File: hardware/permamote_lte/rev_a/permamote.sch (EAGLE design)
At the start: 115 parts, among them IC1 NRF9160, J1 TC2030-JLINK-NL, J2 U.FL-R-SMT, J3 NANO_SIM, J4 U.FL-R-SMT, J5 DM3AT-SF-PEJM5, Q1 PMDXB950UPEL, Q10 PMDXB950UPEL, Q2 PMDXB950UPEL, Q3 PMDXB950UPEL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

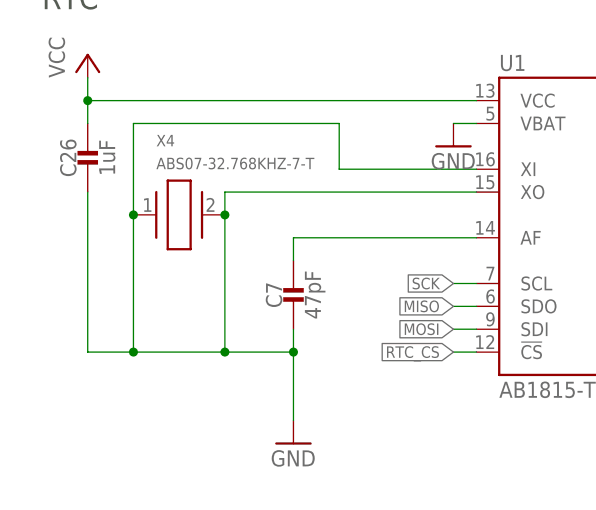
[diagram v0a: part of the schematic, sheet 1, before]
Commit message: more board fixes
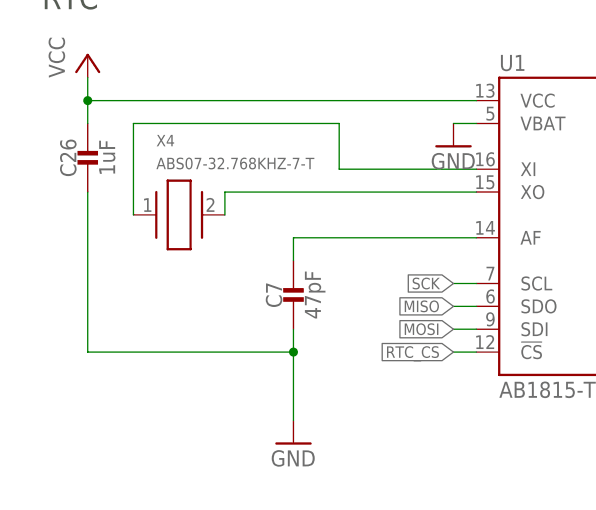
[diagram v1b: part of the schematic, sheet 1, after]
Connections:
- new net N$40: U1.XO, X4.2
- new net N$43: U1.XI, X4.1
- net GND: no longer U1.XI, U1.XO, X4.1, X4.2
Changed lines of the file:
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@@
 </segment>
 <segment>
+<pinref part="GND13" gate="1" pin="GND"/>
 <pinref part="C7" gate="G$1" pin="2"/>
 <wire x1="30.48" y1="17.78" x2="30.48" y2="15.24" width="0.1524" layer="91"/>
-<pinref part="GND13" gate="1" pin="GND"/>
 <wire x1="30.48" y1="15.24" x2="30.48" y2="7.62" width="0.1524" layer="91"/>
+<junction x="30.48" y="15.24"/>
+<pinref part="C26" gate="G$1" pin="2"/>
 <wire x1="7.62" y1="33.02" x2="7.62" y2="15.24" width="0.1524" layer="91"/>
-<wire x1="7.62" y1="15.24" x2="12.7" y2="15.24" width="0.1524" layer="91"/>
-<junction x="30.48" y="15.24"/>
-<wire x1="12.7" y1="15.24" x2="22.86" y2="15.24" width="0.1524" layer="91"/>
-<wire x1="22.86" y1="15.24" x2="30.48" y2="15.24" width="0.1524" layer="91"/>
-<junction x="12.7" y="15.24"/>
-<junction x="22.86" y="15.24"/>
-<pinref part="C26" gate="G$1" pin="2"/>
-<pinref part="X4" gate="G$1" pin="1"/>
-<wire x1="12.7" y1="30.48" x2="12.7" y2="40.64" width="0.1524" layer="91"/>
-<junction x="12.7" y="30.48"/>
-<wire x1="12.7" y1="40.64" x2="35.56" y2="40.64" width="0.1524" layer="91"/>
-<wire x1="35.56" y1="40.64" x2="35.56" y2="35.56" width="0.1524" layer="91"/>
-<pinref part="U1" gate="G$1" pin="XI"/>
-<wire x1="35.56" y1="35.56" x2="50.8" y2="35.56" width="0.1524" layer="91"/>
-<wire x1="12.7" y1="30.48" x2="12.7" y2="15.24" width="0.1524" layer="91"/>
-<pinref part="X4" gate="G$1" pin="2"/>
-<pinref part="U1" gate="G$1" pin="XO"/>
-<wire x1="50.8" y1="33.02" x2="22.86" y2="33.02" width="0.1524" layer="91"/>
-<wire x1="22.86" y1="33.02" x2="22.86" y2="30.48" width="0.1524" layer="91"/>
-<junction x="22.86" y="30.48"/>
-<wire x1="22.86" y1="30.48" x2="22.86" y2="15.24" width="0.1524" layer="91"/>
+<wire x1="7.62" y1="15.24" x2="30.48" y2="15.24" width="0.1524" layer="91"/>
 </segment>
 <segment>
@@
 </segment>
 </net>
+<net name="N$40" class="0">
+<segment>
+<pinref part="X4" gate="G$1" pin="2"/>
+<pinref part="U1" gate="G$1" pin="XO"/>
+<wire x1="50.8" y1="33.02" x2="22.86" y2="33.02" width="0.1524" layer="91"/>
+<wire x1="22.86" y1="33.02" x2="22.86" y2="30.48" width="0.1524" layer="91"/>
+</segment>
+</net>
+<net name="N$43" class="0">
+<segment>
+<pinref part="X4" gate="G$1" pin="1"/>
+<wire x1="12.7" y1="30.48" x2="12.7" y2="40.64" width="0.1524" layer="91"/>
+<wire x1="12.7" y1="40.64" x2="35.56" y2="40.64" width="0.1524" layer="91"/>
+<wire x1="35.56" y1="40.64" x2="35.56" y2="35.56" width="0.1524" layer="91"/>
+<pinref part="U1" gate="G$1" pin="XI"/>
+<wire x1="35.56" y1="35.56" x2="50.8" y2="35.56" width="0.1524" layer="91"/>
+</segment>
+</net>

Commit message: got rid of erc errors
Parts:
- C3, C4: value (none) -> DNP
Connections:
- removed net +3V3: R19.2, U10.VSUPP
- removed net N$3: IC1.SIM_DET
- removed net N$33: IC1.SIM_1V8
- removed net N$42: IC1.SIM_RST
- removed net N$6: U4.PON
- removed net N$7: C37.1, IC1.VDD_GPIO
- net GPS_EN: now also U4.PON
- net SIM_1V8: now also IC1.SIM_1V8
- net SIM_RST: now also IC1.SIM_RST
- net VCC: now also C37.1, IC1.VDD_GPIO, R19.2, U10.VSUPP
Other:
- moved on the sheet: U4
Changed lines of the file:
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@@
 <part name="GND32" library="supply1" library_urn="urn:adsk.eagle:library:371" deviceset="GND" device=""/>
 <part name="IC1" library="nRF9160" deviceset="NRF9160" device=""/>
-<part name="C3" library="passives" deviceset="CAPACITOR" device="0402_CAP"/>
-<part name="C4" library="passives" deviceset="CAPACITOR" device="0402_CAP"/>
+<part name="C3" library="passives" deviceset="CAPACITOR" device="0402_CAP" value="DNP"/>
+<part name="C4" library="passives" deviceset="CAPACITOR" device="0402_CAP" value="DNP"/>
 <part name="GND33" library="supply1" library_urn="urn:adsk.eagle:library:371" deviceset="GND" device=""/>
 <part name="U4" library="Particle" deviceset="BGA725L6" device=""/>
@@
 <attribute name="DESCRIPTION" value="IC LOAD SWITCH SOT23-6"/>
 </part>
-<part name="+3V8" library="regulators" deviceset="+3V3" device=""/>
 <part name="FRAME4" library="lab11-frames" deviceset="LETTER_L_BLANK" device="">
 <attribute name="AUTHOR" value="MEGHNA MANDAVA"/>
@@
 <part name="GND39" library="supply1" library_urn="urn:adsk.eagle:library:371" deviceset="GND" device=""/>
 <part name="GND40" library="supply1" library_urn="urn:adsk.eagle:library:371" deviceset="GND" device=""/>
+<part name="P+13" library="supply1" library_urn="urn:adsk.eagle:library:371" deviceset="VCC" device=""/>
 </parts>
 <sheets>
@@
 <attribute name="VALUE" x="213.36" y="121.92" size="1.778" layer="96"/>
 </instance>
-<instance part="U4" gate="G$1" x="162.56" y="149.86" smashed="yes" rot="R180">
-<attribute name="NAME" x="172.72" y="133.35" size="1.778" layer="95" rot="R180"/>
-<attribute name="VALUE" x="172.72" y="170.18" size="1.778" layer="96" rot="MR0"/>
+<instance part="U4" gate="G$1" x="167.64" y="149.86" smashed="yes" rot="R180">
+<attribute name="NAME" x="177.8" y="133.35" size="1.778" layer="95" rot="R180"/>
+<attribute name="VALUE" x="177.8" y="170.18" size="1.778" layer="96" rot="MR0"/>
 </instance>
 <instance part="L2" gate="G$1" x="226.06" y="149.86" smashed="yes" rot="R90">
@@
 <pinref part="GND1" gate="1" pin="GND"/>
 <pinref part="U4" gate="G$1" pin="GND@1"/>
-<wire x1="142.24" y1="154.94" x2="149.86" y2="154.94" width="0.1524" layer="91"/>
+<wire x1="142.24" y1="154.94" x2="154.94" y2="154.94" width="0.1524" layer="91"/>
 </segment>
 <segment>
 <pinref part="U4" gate="G$1" pin="GND@4"/>
-<wire x1="175.26" y1="144.78" x2="185.42" y2="144.78" width="0.1524" layer="91"/>
+<wire x1="180.34" y1="144.78" x2="185.42" y2="144.78" width="0.1524" layer="91"/>
 <pinref part="GND2" gate="1" pin="GND"/>
 <wire x1="185.42" y1="144.78" x2="185.42" y2="139.7" width="0.1524" layer="91"/>
@@
 <wire x1="7.62" y1="45.72" x2="7.62" y2="43.18" width="0.1524" layer="91"/>
 <junction x="7.62" y="43.18"/>
+<wire x1="7.62" y1="45.72" x2="7.62" y2="43.18" width="0.1524" layer="91"/>
 </segment>
 <segment>
@@
 <pinref part="U4" gate="G$1" pin="VCC"/>
 <wire x1="137.16" y1="152.4" x2="137.16" y2="149.86" width="0.1524" layer="91"/>
-<wire x1="137.16" y1="149.86" x2="149.86" y2="149.86" width="0.1524" layer="91"/>
+<wire x1="137.16" y1="149.86" x2="154.94" y2="149.86" width="0.1524" layer="91"/>
+</segment>
+<segment>
+<pinref part="P+24" gate="VCC" pin="VCC"/>
+<pinref part="C37" gate="G$1" pin="1"/>
+<wire x1="20.32" y1="119.38" x2="53.34" y2="119.38" width="0.1524" layer="91"/>
+<wire x1="20.32" y1="116.84" x2="20.32" y2="119.38" width="0.1524" layer="91"/>
+<junction x="20.32" y="119.38"/>
+<wire x1="20.32" y1="119.38" x2="12.7" y2="119.38" width="0.1524" layer="91"/>
+<wire x1="12.7" y1="119.38" x2="12.7" y2="124.46" width="0.1524" layer="91"/>
+<pinref part="IC1" gate="G$1" pin="VDD_GPIO"/>
 </segment>
 </net>
@@
 <label x="134.62" y="86.36" size="1.27" layer="95" rot="R270" xref="yes"/>
 </segment>
-</net>
-<net name="N$33" class="0">
 <segment>
 <wire x1="134.62" y1="86.36" x2="134.62" y2="88.9" width="0.1524" layer="91"/>
@@
 </segment>
 </net>
-<net name="N$42" class="0">
-<segment>
-<wire x1="124.46" y1="86.36" x2="124.46" y2="88.9" width="0.1524" layer="91"/>
-<pinref part="IC1" gate="G$1" pin="SIM_RST"/>
-</segment>
-</net>
 <net name="N$2" class="0">
 <segment>
 <pinref part="L1" gate="G$1" pin="1"/>
 <pinref part="U4" gate="G$1" pin="AI"/>
-<wire x1="182.88" y1="149.86" x2="175.26" y2="149.86" width="0.1524" layer="91"/>
+<wire x1="182.88" y1="149.86" x2="180.34" y2="149.86" width="0.1524" layer="91"/>
 </segment>
 </net>
@@
 <wire x1="144.78" y1="114.3" x2="147.32" y2="114.3" width="0.1524" layer="91"/>
 <label x="147.32" y="114.3" size="1.27" layer="95" xref="yes"/>
-<label x="180.34" y="154.94" size="1.27" layer="95" xref="yes"/>
 <pinref part="IC1" gate="G$1" pin="MAGPIO0"/>
+</segment>
+<segment>
+<pinref part="U4" gate="G$1" pin="PON"/>
+<wire x1="190.5" y1="154.94" x2="180.34" y2="154.94" width="0.1524" layer="91"/>
+<label x="190.5" y="154.94" size="1.778" layer="95" xref="yes"/>
 </segment>
 </net>
@@
 </segment>
 </net>
-<net name="N$7" class="0">
-<segment>
-<pinref part="P+24" gate="VCC" pin="VCC"/>
-<pinref part="C37" gate="G$1" pin="1"/>
-<wire x1="20.32" y1="119.38" x2="53.34" y2="119.38" width="0.1524" layer="91"/>
-<wire x1="20.32" y1="116.84" x2="20.32" y2="119.38" width="0.1524" layer="91"/>
-<junction x="20.32" y="119.38"/>
-<wire x1="20.32" y1="119.38" x2="12.7" y2="119.38" width="0.1524" layer="91"/>
-<wire x1="12.7" y1="119.38" x2="12.7" y2="124.46" width="0.1524" layer="91"/>
-<pinref part="IC1" gate="G$1" pin="VDD_GPIO"/>
-</segment>
-</net>
-<net name="N$6" class="0">
-<segment>
-<pinref part="U4" gate="G$1" pin="PON"/>
-<wire x1="180.34" y1="154.94" x2="175.26" y2="154.94" width="0.1524" layer="91"/>
-</segment>
-</net>
-<net name="N$1" class="0">
-<segment>
-<pinref part="IC1" gate="G$1" pin="GPS"/>
-<pinref part="U4" gate="G$1" pin="AO"/>
-<wire x1="144.78" y1="139.7" x2="144.78" y2="142.24" width="0.1524" layer="91"/>
-<wire x1="144.78" y1="139.7" x2="144.78" y2="144.78" width="0.1524" layer="91"/>
-<wire x1="144.78" y1="144.78" x2="149.86" y2="144.78" width="0.1524" layer="91"/>
-</segment>
-</net>
-<net name="N$3" class="0">
-<segment>
-<pinref part="IC1" gate="G$1" pin="SIM_DET"/>
-<wire x1="127" y1="88.9" x2="127" y2="86.36" width="0.1524" layer="91"/>
-</segment>
-</net>
 <net name="SIM_IO" class="0">
 <segment>
@@
 <segment>
 <label x="124.46" y="86.36" size="1.27" layer="95" rot="R270" xref="yes"/>
+</segment>
+<segment>
+<wire x1="124.46" y1="86.36" x2="124.46" y2="88.9" width="0.1524" layer="91"/>
+<pinref part="IC1" gate="G$1" pin="SIM_RST"/>
 </segment>
 </net>
@@
 <pinref part="U1" gate="G$1" pin="XI"/>
 <wire x1="35.56" y1="35.56" x2="50.8" y2="35.56" width="0.1524" layer="91"/>
+</segment>
+</net>
+<net name="N$1" class="0">
+<segment>
+<pinref part="IC1" gate="G$1" pin="GPS"/>
+<wire x1="144.78" y1="139.7" x2="149.86" y2="139.7" width="0.1524" layer="91"/>
+<wire x1="149.86" y1="139.7" x2="149.86" y2="144.78" width="0.1524" layer="91"/>
+<pinref part="U4" gate="G$1" pin="AO"/>
+<wire x1="149.86" y1="144.78" x2="154.94" y2="144.78" width="0.1524" layer="91"/>
 </segment>
 </net>
@@
 <attribute name="VALUE" x="73.66" y="66.294" size="1.778" layer="96"/>
 </instance>
-<instance part="+3V8" gate="P1" x="60.96" y="88.9" smashed="yes">
-<attribute name="VALUE" x="58.42" y="83.82" size="1.778" layer="96" rot="R90"/>
-</instance>
 <instance part="FRAME4" gate="G$1" x="0" y="0" smashed="yes"/>
 <instance part="FRAME4" gate="G$2" x="152.4" y="0" smashed="yes">
@@
 <attribute name="NAME" x="58.7756" y="125.9586" size="2.0828" layer="95" ratio="6" rot="SR0"/>
 <attribute name="VALUE" x="58.1406" y="100.5586" size="2.0828" layer="96" ratio="6" rot="SR0"/>
+</instance>
+<instance part="P+13" gate="VCC" x="60.96" y="88.9" smashed="yes">
+<attribute name="VALUE" x="58.42" y="86.36" size="1.778" layer="96" rot="R90"/>
 </instance>
 </instances>
@@
 </segment>
 </net>
-<net name="+3V3" class="0">
+<net name="VCC" class="0">
 <segment>
 <pinref part="R19" gate="G$1" pin="2"/>
@@
 <wire x1="66.04" y1="73.66" x2="66.04" y2="83.82" width="0.1524" layer="91"/>
 <wire x1="66.04" y1="83.82" x2="60.96" y2="83.82" width="0.1524" layer="91"/>
-<pinref part="+3V8" gate="P1" pin="+3V3"/>
-<wire x1="60.96" y1="83.82" x2="60.96" y2="86.36" width="0.1524" layer="91"/>
+<pinref part="P+13" gate="VCC" pin="VCC"/>
+<wire x1="60.96" y1="86.36" x2="60.96" y2="83.82" width="0.1524" layer="91"/>
 <junction x="60.96" y="83.82"/>
 </segment>
